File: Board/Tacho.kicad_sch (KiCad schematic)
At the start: 16 parts

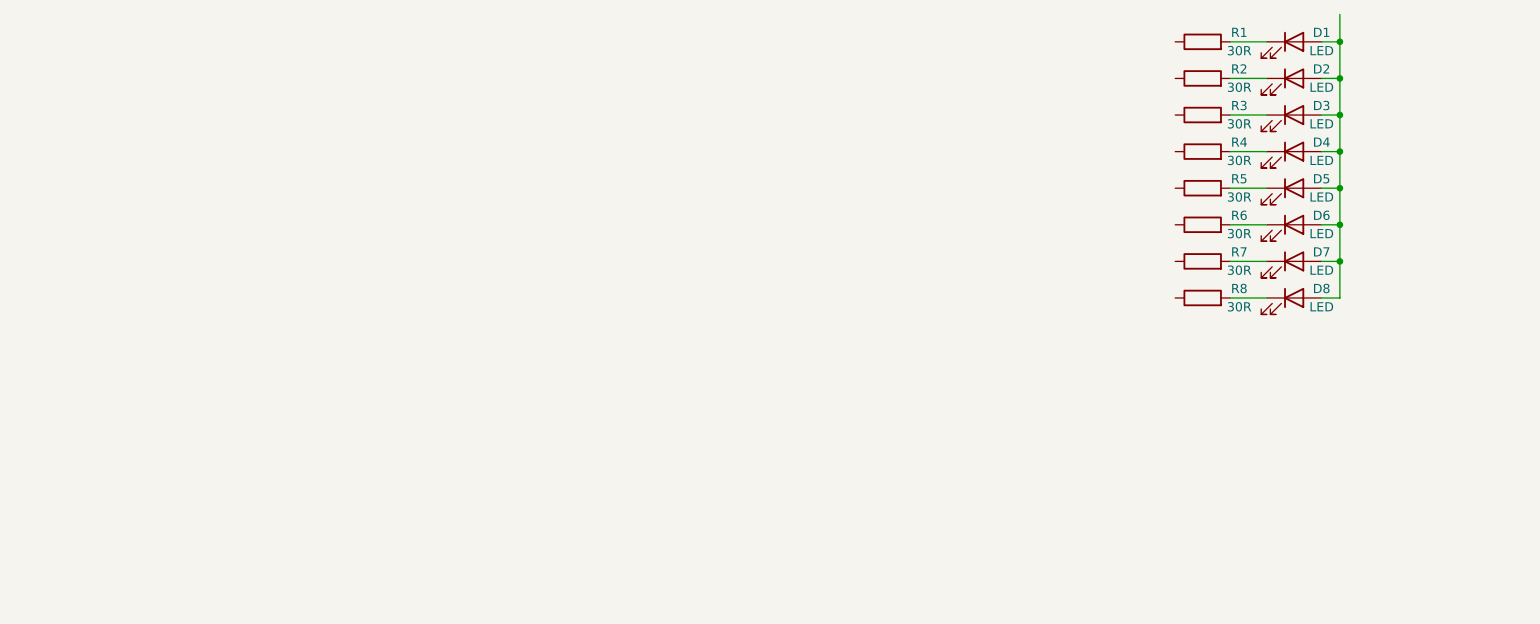
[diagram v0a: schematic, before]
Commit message: Mechanicals added
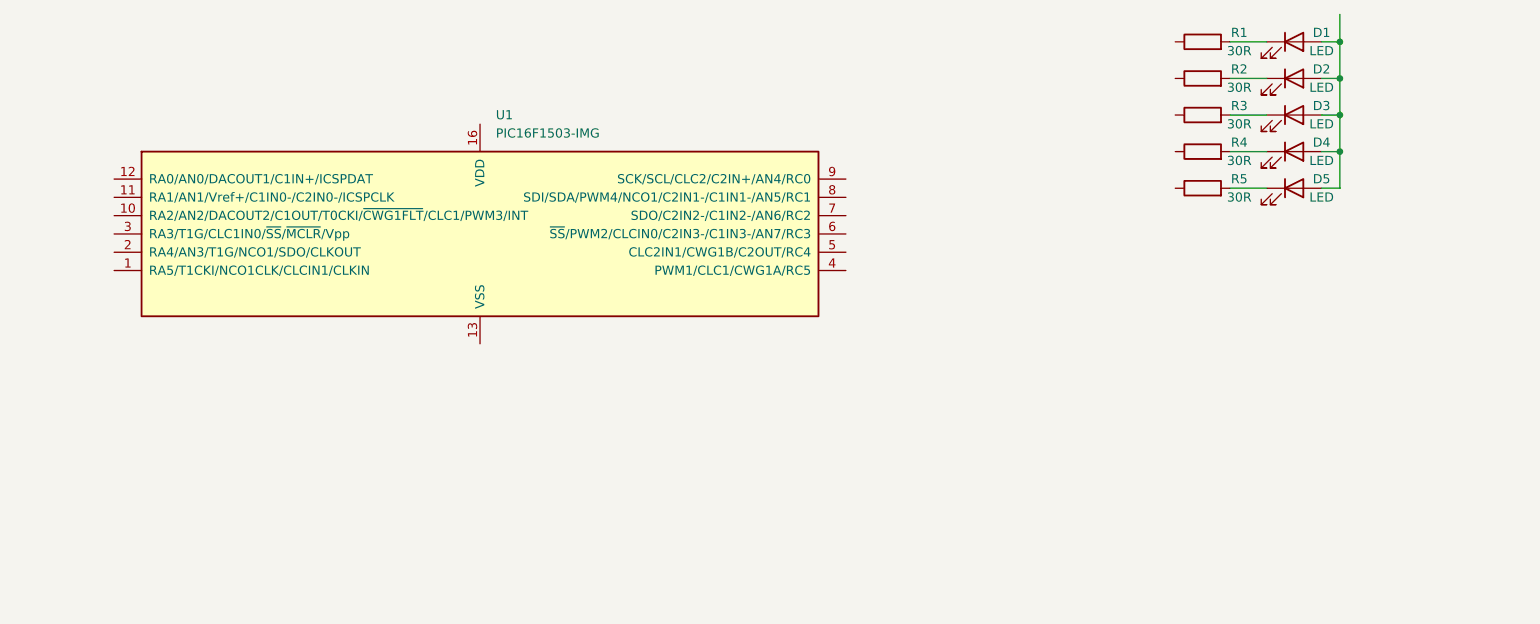
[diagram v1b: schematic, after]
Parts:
- removed D6, D7, D8: LED, LED_SMD:LED_0402_1005Metric, symbol Device:LED
- removed R6, R7, R8: 30R, Resistor_SMD:R_0402_1005Metric, symbol Device:R
- added U1: PIC16F1503-IMG, symbol MCU_Microchip_PIC16:PIC16F1503-IMG
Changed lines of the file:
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@@
   (junction (at 232.41 69.85) (diameter 0) (color 0 0 0 0)
   )
-  (junction (at 232.41 85.09) (diameter 0) (color 0 0 0 0)
-  )
-  (junction (at 232.41 74.93) (diameter 0) (color 0 0 0 0)
-  )
-  (junction (at 232.41 80.01) (diameter 0) (color 0 0 0 0)
-  )
   (junction (at 232.41 64.77) (diameter 0) (color 0 0 0 0)
   )
@@
     (stroke (width 0) (type default))
   )
-  (wire (pts (xy 217.17 85.09) (xy 222.25 85.09))
-    (stroke (width 0) (type default))
-  )
   (wire (pts (xy 232.41 59.69) (xy 232.41 64.77))
     (stroke (width 0) (type default))
   )
-  (wire (pts (xy 229.87 90.17) (xy 232.41 90.17))
-    (stroke (width 0) (type default))
-  )
-  (wire (pts (xy 232.41 85.09) (xy 232.41 90.17))
-    (stroke (width 0) (type default))
-  )
   (wire (pts (xy 217.17 64.77) (xy 222.25 64.77))
     (stroke (width 0) (type default))
   )
-  (wire (pts (xy 229.87 80.01) (xy 232.41 80.01))
-    (stroke (width 0) (type default))
-  )
-  (wire (pts (xy 217.17 90.17) (xy 222.25 90.17))
-    (stroke (width 0) (type default))
-  )
   (wire (pts (xy 229.87 54.61) (xy 232.41 54.61))
     (stroke (width 0) (type default))
@@
     (stroke (width 0) (type default))
   )
-  (wire (pts (xy 217.17 80.01) (xy 222.25 80.01))
-    (stroke (width 0) (type default))
-  )
   (wire (pts (xy 229.87 74.93) (xy 232.41 74.93))
     (stroke (width 0) (type default))
   )
-  (wire (pts (xy 229.87 85.09) (xy 232.41 85.09))
-    (stroke (width 0) (type default))
-  )
-  (wire (pts (xy 232.41 74.93) (xy 232.41 80.01))
-    (stroke (width 0) (type default))
-  )
   (wire (pts (xy 217.17 69.85) (xy 222.25 69.85))
     (stroke (width 0) (type default))
@@
     (stroke (width 0) (type default))
   )
-  (wire (pts (xy 232.41 80.01) (xy 232.41 85.09))
-    (stroke (width 0) (type default))
-  )
   (symbol (lib_id "Device:LED") (at 226.06 64.77 0) (unit 1)
     (in_bom yes) (on_board yes) (dnp no)
@@
     )
   )
-  (symbol (lib_id "Device:LED") (at 226.06 90.17 0) (unit 1)
-    (in_bom yes) (on_board yes) (dnp no)
-    (property "Reference" "D8" (at 229.87 88.9 0)
-      (effects (font (size 1.27 1.27)))
-    )
-    (property "Value" "LED" (at 229.87 91.44 0)
-      (effects (font (size 1.27 1.27)))
-    )
-    (property "Footprint" "LED_SMD:LED_0402_1005Metric" (at 226.06 90.17 0)
-      (effects (font (size 1.27 1.27)) hide)
-    )
-    (property "Datasheet" "~" (at 226.06 90.17 0)
-      (effects (font (size 1.27 1.27)) hide)
-    )
-    (pin "1")
-    (pin "2")
-    (instances
-      (project "Tacho"
-        (path "/95fca9cd-8dfb-486f-9bd1-0f8eec0c6c0c"
-          (reference "D8") (unit 1)
-        )
-      )
-    )
-  )
-  (symbol (lib_id "Device:R") (at 213.36 90.17 90) (unit 1)
-    (in_bom yes) (on_board yes) (dnp no)
-    (property "Reference" "R8" (at 218.44 88.9 90)
-      (effects (font (size 1.27 1.27)))
-    )
-    (property "Value" "30R" (at 218.44 91.44 90)
-      (effects (font (size 1.27 1.27)))
-    )
-    (property "Footprint" "Resistor_SMD:R_0402_1005Metric" (at 213.36 91.948 90)
-      (effects (font (size 1.27 1.27)) hide)
-    )
-    (property "Datasheet" "~" (at 213.36 90.17 0)
-      (effects (font (size 1.27 1.27)) hide)
-    )
-    (pin "1")
-    (pin "2")
-    (instances
-      (project "Tacho"
-        (path "/95fca9cd-8dfb-486f-9bd1-0f8eec0c6c0c"
-          (reference "R8") (unit 1)
-        )
-      )
-    )
-  )
   (symbol (lib_id "Device:R") (at 213.36 64.77 90) (unit 1)
     (in_bom yes) (on_board yes) (dnp no)
@@
     )
   )
-  (symbol (lib_id "Device:LED") (at 226.06 80.01 0) (unit 1)
-    (in_bom yes) (on_board yes) (dnp no)
-    (property "Reference" "D6" (at 229.87 78.74 0)
-      (effects (font (size 1.27 1.27)))
-    )
-    (property "Value" "LED" (at 229.87 81.28 0)
-      (effects (font (size 1.27 1.27)))
-    )
-    (property "Footprint" "LED_SMD:LED_0402_1005Metric" (at 226.06 80.01 0)
-      (effects (font (size 1.27 1.27)) hide)
-    )
-    (property "Datasheet" "~" (at 226.06 80.01 0)
-      (effects (font (size 1.27 1.27)) hide)
-    )
-    (pin "1")
-    (pin "2")
-    (instances
-      (project "Tacho"
-        (path "/95fca9cd-8dfb-486f-9bd1-0f8eec0c6c0c"
-          (reference "D6") (unit 1)
-        )
-      )
-    )
-  )
-  (symbol (lib_id "Device:R") (at 213.36 80.01 90) (unit 1)
-    (in_bom yes) (on_board yes) (dnp no)
-    (property "Reference" "R6" (at 218.44 78.74 90)
-      (effects (font (size 1.27 1.27)))
-    )
-    (property "Value" "30R" (at 218.44 81.28 90)
-      (effects (font (size 1.27 1.27)))
-    )
-    (property "Footprint" "Resistor_SMD:R_0402_1005Metric" (at 213.36 81.788 90)
-      (effects (font (size 1.27 1.27)) hide)
-    )
-    (property "Datasheet" "~" (at 213.36 80.01 0)
-      (effects (font (size 1.27 1.27)) hide)
-    )
-    (pin "1")
-    (pin "2")
-    (instances
-      (project "Tacho"
-        (path "/95fca9cd-8dfb-486f-9bd1-0f8eec0c6c0c"
-          (reference "R6") (unit 1)
+  (symbol (lib_id "MCU_Microchip_PIC16:PIC16F1503-IMG") (at 113.03 81.28 0) (unit 1)
+    (in_bom yes) (on_board yes) (dnp no) (fields_autoplaced)
+    (property "Reference" "U1" (at 115.2241 64.77 0)
+      (effects (font (size 1.27 1.27)) (justify left))
+    )
+    (property "Value" "PIC16F1503-IMG" (at 115.2241 67.31 0)
+      (effects (font (size 1.27 1.27)) (justify left))
+    )
+    (property "Footprint" "" (at 113.03 81.28 0)
+      (effects (font (size 1.27 1.27)) hide)
+    )
+    (property "Datasheet" "http://ww1.microchip.com/downloads/en/DeviceDoc/41607A.pdf" (at 113.03 81.28 0)
+      (effects (font (size 1.27 1.27)) hide)
+    )
+    (pin "11")
+    (pin "12")
+    (pin "4")
+    (pin "3")
+    (pin "9")
+    (pin "2")
+    (pin "7")
+    (pin "8")
+    (pin "10")
+    (pin "1")
+    (pin "5")
+    (pin "6")
+    (pin "13")
+    (pin "16")
+    (instances
+      (project "Tacho"
+        (path "/95fca9cd-8dfb-486f-9bd1-0f8eec0c6c0c"
+          (reference "U1") (unit 1)
         )
       )
@@
     )
   )
-  (symbol (lib_id "Device:LED") (at 226.06 85.09 0) (unit 1)
-    (in_bom yes) (on_board yes) (dnp no)
-    (property "Reference" "D7" (at 229.87 83.82 0)
-      (effects (font (size 1.27 1.27)))
-    )
-    (property "Value" "LED" (at 229.87 86.36 0)
-      (effects (font (size 1.27 1.27)))
-    )
-    (property "Footprint" "LED_SMD:LED_0402_1005Metric" (at 226.06 85.09 0)
-      (effects (font (size 1.27 1.27)) hide)
-    )
-    (property "Datasheet" "~" (at 226.06 85.09 0)
-      (effects (font (size 1.27 1.27)) hide)
-    )
-    (pin "1")
-    (pin "2")
-    (instances
-      (project "Tacho"
-        (path "/95fca9cd-8dfb-486f-9bd1-0f8eec0c6c0c"
-          (reference "D7") (unit 1)
-        )
-      )
-    )
-  )
   (symbol (lib_id "Device:R") (at 213.36 69.85 90) (unit 1)
     (in_bom yes) (on_board yes) (dnp no)
@@
         )
       )
-    )
-  )
-  (symbol (lib_id "Device:R") (at 213.36 85.09 90) (unit 1)
-    (in_bom yes) (on_board yes) (dnp no)
-    (property "Reference" "R7" (at 218.44 83.82 90)
-      (effects (font (size 1.27 1.27)))
-    )
-    (property "Value" "30R" (at 218.44 86.36 90)
-      (effects (font (size 1.27 1.27)))
-    )
-    (property "Footprint" "Resistor_SMD:R_0402_1005Metric" (at 213.36 86.868 90)
-      (effects (font (size 1.27 1.27)) hide)
-    )
-    (property "Datasheet" "~" (at 213.36 85.09 0)
-      (effects (font (size 1.27 1.27)) hide)
-    )
-    (pin "1")
-    (pin "2")
-    (instances
-      (project "Tacho"
-        (path "/95fca9cd-8dfb-486f-9bd1-0f8eec0c6c0c"
-          (reference "R7") (unit 1)
-        )
-      )

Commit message: Schematic done
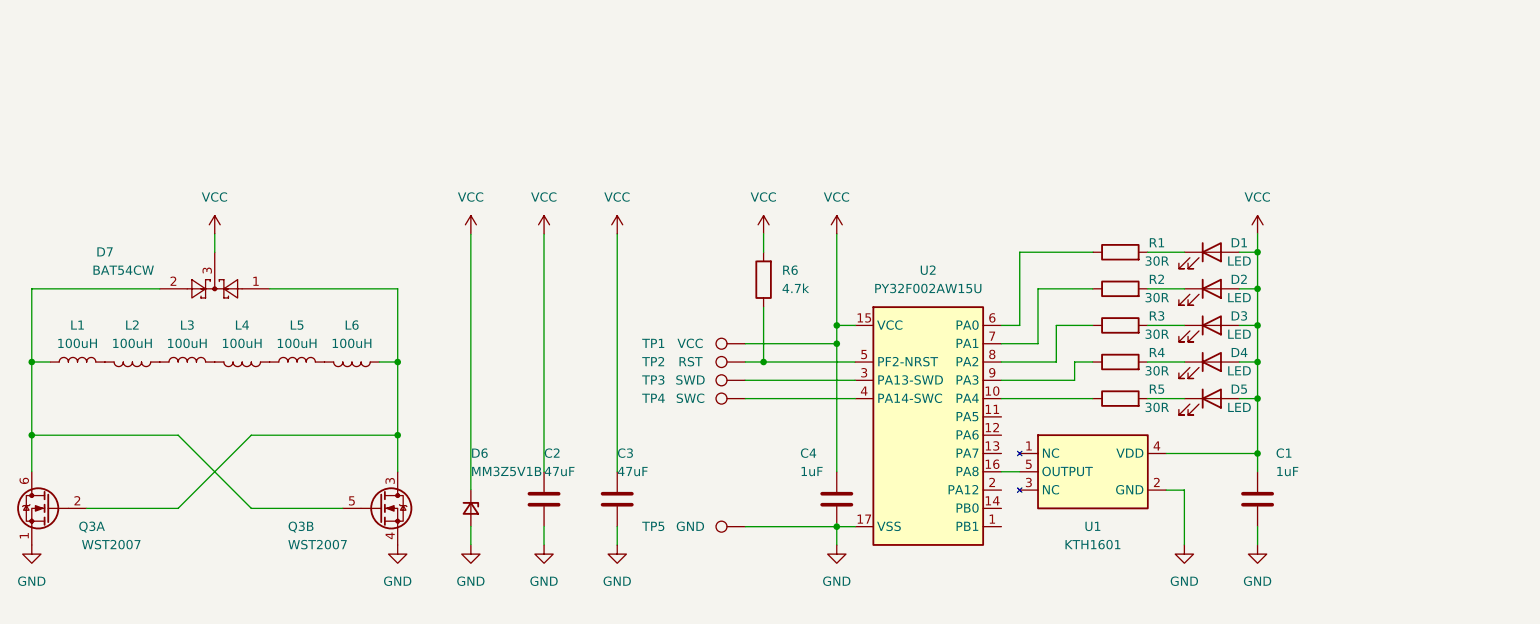
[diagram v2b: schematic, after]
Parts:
- removed U1: PIC16F1503-IMG, symbol MCU_Microchip_PIC16:PIC16F1503-IMG
- added C1, C4: 1uF, Capacitor_SMD:C_0402_1005Metric_Pad0.74x0.62mm_HandSolder, symbol Device:C
- added C2, C3: 47uF, Capacitor_SMD:C_0805_2012Metric_Pad1.18x1.45mm_HandSolder, symbol Device:C
- added D6: MM3Z5V1B, Diode_SMD:D_SOD-323, symbol Device:D_Zener_Small
- added D7: BAT54CW, Package_TO_SOT_SMD:SOT-323_SC-70, symbol Diode:BAT54CW
- added L1, L2, L3, L4, L5, L6: 100uH, USER:L_SHOUHAN _CY43-100UH, symbol Device:L
- added Q3: WST2007, Package_TO_SOT_SMD:SOT-363_SC-70-6, symbol USER:WST2007
- added R6: 4.7k, Resistor_SMD:R_0402_1005Metric, symbol Device:R
- added TP1: VCC, TestPoint:TestPoint_Pad_D2.0mm, symbol Connector:TestPoint
- added TP2: RST, TestPoint:TestPoint_Pad_D2.0mm, symbol Connector:TestPoint
- added TP3: SWD, TestPoint:TestPoint_Pad_D2.0mm, symbol Connector:TestPoint
- added TP4: SWC, TestPoint:TestPoint_Pad_D2.0mm, symbol Connector:TestPoint
- added TP5: GND, TestPoint:TestPoint_Pad_D2.0mm, symbol Connector:TestPoint
- added U1: KTH1601, Package_TO_SOT_SMD:SOT-553, symbol USER:KTH1601
- added U2: PY32F002AW15U, Package_DFN_QFN:QFN-16-1EP_3x3mm_P0.5mm_EP1.7x1.7mm, symbol USER:PY32F002AW15U
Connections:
- net VCC: now reaches D1.2 (A), D2.2 (A), D3.2 (A), D4.2 (A), D5.2 (A)
- net VCC: now also C1.1, C2.1, C3.1, C4.1, D6.1 (K), D7.3, R6.2, TP1.1, U1.4 (VDD), U2.15 (VCC)
- net at R3.1: now also U2.8 (PA2)
- net at R5.1: now also U2.10 (PA4)
- net at R4.1: now also U2.9 (PA3)
- net at R1.1: now also U2.6 (PA0)
- net at R2.1: now also U2.7 (PA1)
- new net: D7.1, L6.1, Q3.2 (G), Q3.3 (D)
- new net: L5.2, L6.2
- new net: D7.2, L1.1, Q3.5 (G), Q3.6 (D)
- new net: L1.2, L2.2
- new net: TP4.1, U2.4 (PA14-SWC)
- new net: TP3.1, U2.3 (PA13-SWD)
- new net: L4.1, L5.1
- new net: L2.1, L3.1
- new net: L3.2, L4.2
- new net: U1.5 (OUTPUT), U2.16 (PA8)
- new net: R6.1, TP2.1, U2.5 (PF2-NRST)
- new net GND: C1.2, C2.2, C3.2, C4.2, D6.2 (A), Q3.1 (S), Q3.4 (S), TP5.1, U1.2 (GND), U2.17 (VSS)
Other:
- moved on the sheet: D1, D2, D3, D4, D5, R1, R2, R3, R4, R5

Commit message: Layout finished
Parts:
- removed U1: KTH1601, Package_TO_SOT_SMD:SOT-553, symbol USER:KTH1601
- added C5: 1uF, Capacitor_SMD:C_0402_1005Metric_Pad0.74x0.62mm_HandSolder, symbol Device:C
- added R7: 10k, Resistor_SMD:R_0402_1005Metric, symbol Device:R
- added U3: DRV5013, Package_TO_SOT_SMD:SOT-23, symbol USER:DRV5013
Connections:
- net GND: now also C5.2, U3.3 (GND)
- net VCC: now also R7.2, U3.1 (VCC)
- net at U2.16 (PA8): now also C5.1, R7.1, U3.2 (OUT)
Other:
- moved on the sheet: C1, C2, C3, C4, D1, D2, D3, D4, D5, D6, R1, R2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

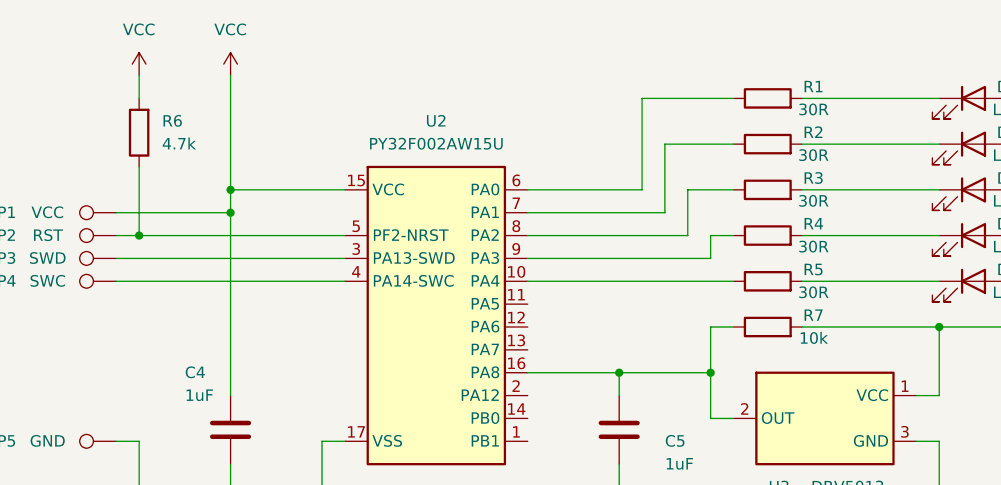
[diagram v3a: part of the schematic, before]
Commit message: Current limit and reset pullup resistors value changed
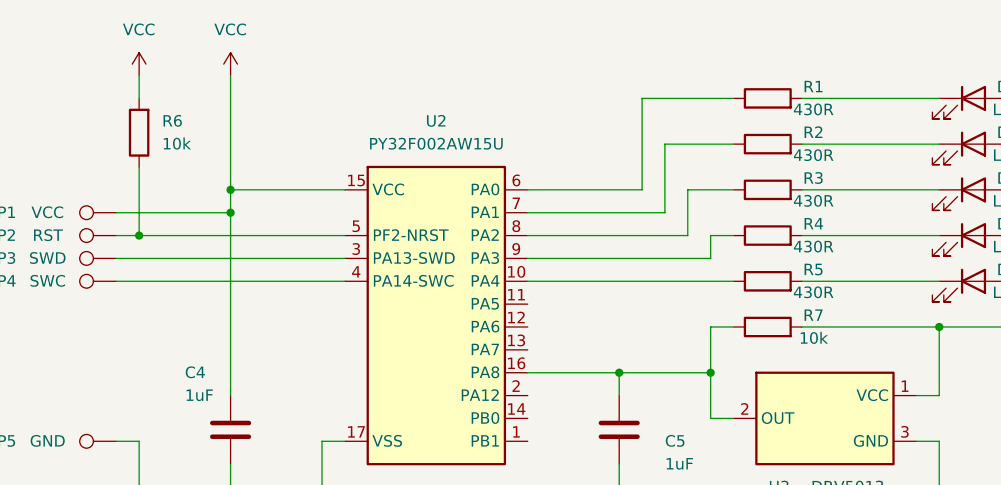
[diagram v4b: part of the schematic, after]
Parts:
- R1, R2, R3, R4, R5: value 30R -> 430R
- R6: value 4.7k -> 10k
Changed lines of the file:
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@@
       (effects (font (size 1.27 1.27)))
     )
-    (property "Value" "30R" (at 227.33 95.25 90)
+    (property "Value" "430R" (at 227.33 95.25 90)
       (effects (font (size 1.27 1.27)))
     )
@@
       (effects (font (size 1.27 1.27)))
     )
-    (property "Value" "30R" (at 227.33 105.41 90)
+    (property "Value" "430R" (at 227.33 105.41 90)
       (effects (font (size 1.27 1.27)))
     )
@@
       (effects (font (size 1.27 1.27)))
     )
-    (property "Value" "30R" (at 227.33 100.33 90)
+    (property "Value" "430R" (at 227.33 100.33 90)
       (effects (font (size 1.27 1.27)))
     )
@@
       (effects (font (size 1.27 1.27)))
     )
-    (property "Value" "30R" (at 227.33 85.09 90)
+    (property "Value" "430R" (at 227.33 85.09 90)
       (effects (font (size 1.27 1.27)))
     )
@@
       (effects (font (size 1.27 1.27)))
     )
-    (property "Value" "30R" (at 227.33 90.17 90)
+    (property "Value" "430R" (at 227.33 90.17 90)
       (effects (font (size 1.27 1.27)))
     )
@@
       (effects (font (size 1.27 1.27)) (justify right))
     )
-    (property "Value" "4.7k" (at 154.94 88.9 0)
+    (property "Value" "10k" (at 154.94 88.9 0)
       (effects (font (size 1.27 1.27)) (justify right))
     )
